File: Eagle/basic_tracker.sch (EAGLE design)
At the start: 21 parts, among them CN1 BATTERY, IC1 MCP1700 3.3v, X1 SMA

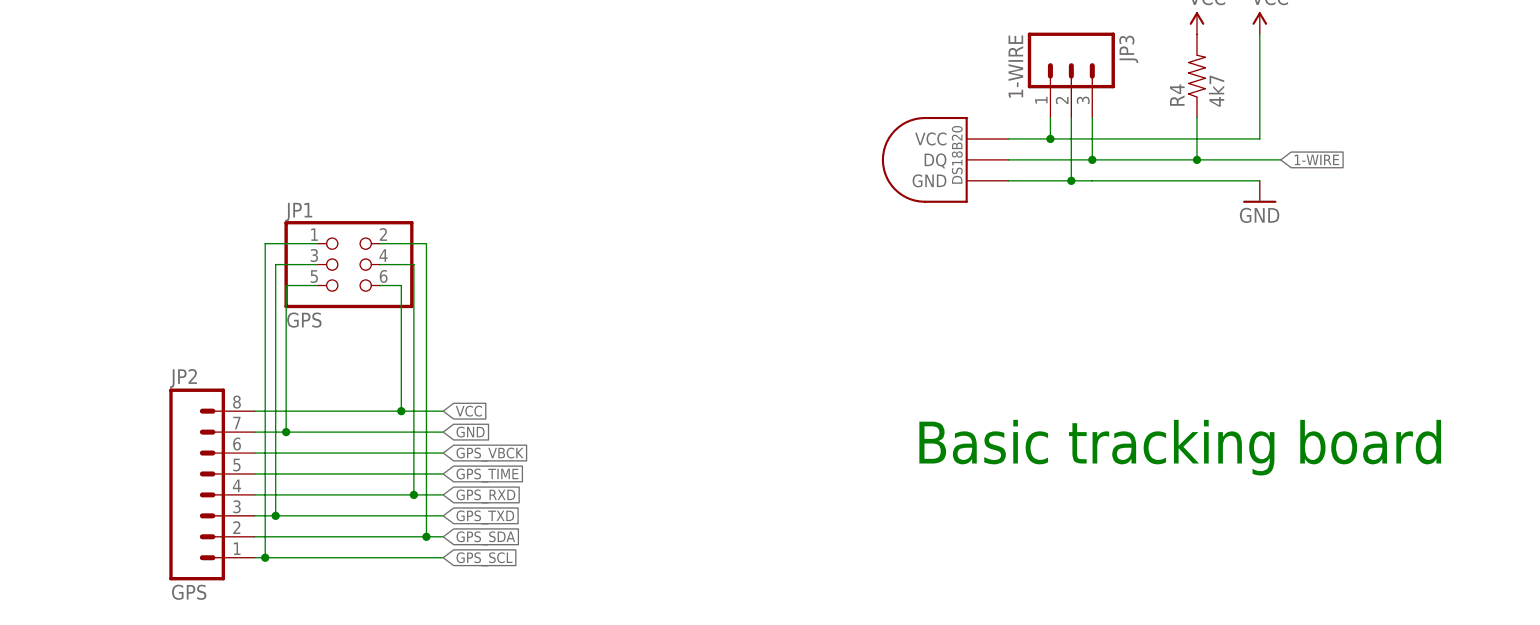
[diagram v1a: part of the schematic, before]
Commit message: Added a slightly modified version of the CAM file, tweaked the board and rerouted a few traces by hand
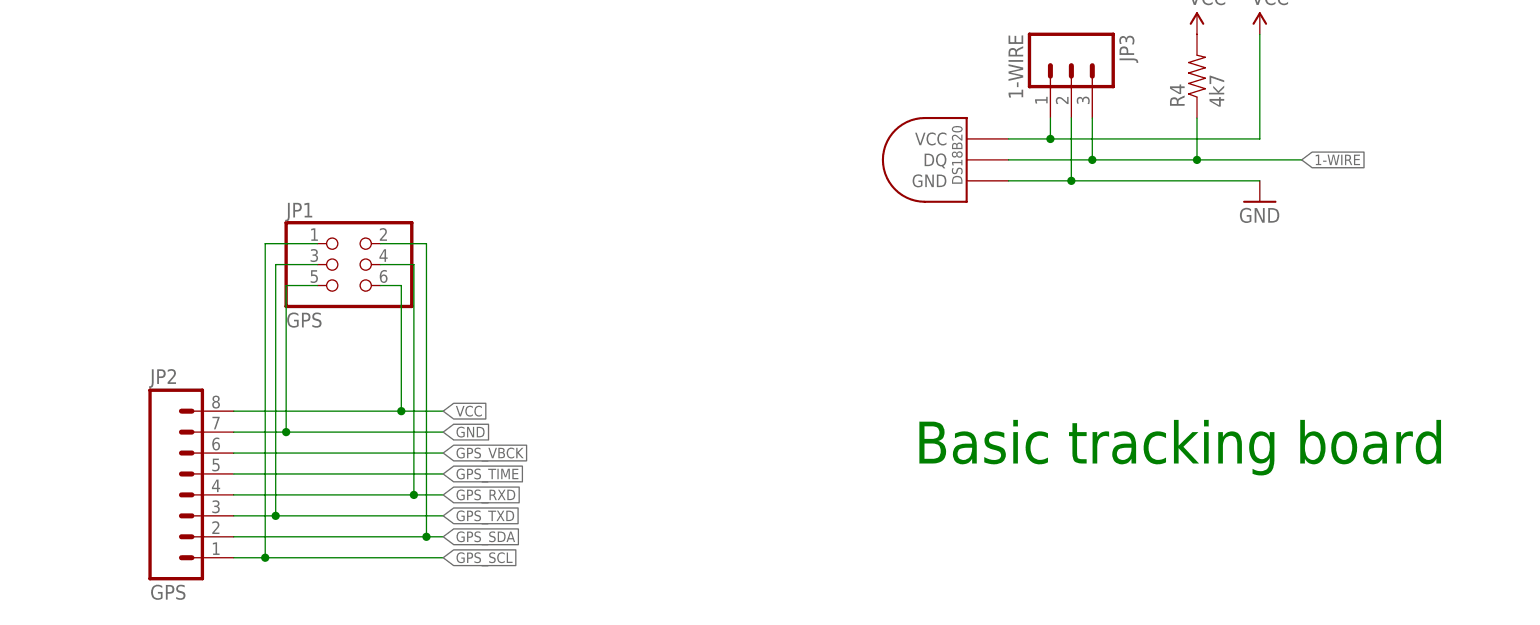
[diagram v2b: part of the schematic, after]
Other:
- moved on the sheet: JP2
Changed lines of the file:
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@@
 <grid distance="0.1" unitdist="inch" unit="inch" style="lines" multiple="1" display="no" altdistance="0.01" altunitdist="inch" altunit="inch"/>
 <layers>
-<layer number="1" name="Top" color="4" fill="1" visible="no" active="no"/>
-<layer number="16" name="Bottom" color="1" fill="1" visible="no" active="no"/>
-<layer number="17" name="Pads" color="2" fill="1" visible="no" active="no"/>
-<layer number="18" name="Vias" color="2" fill="1" visible="no" active="no"/>
-<layer number="19" name="Unrouted" color="6" fill="1" visible="no" active="no"/>
-<layer number="20" name="Dimension" color="7" fill="1" visible="no" active="no"/>
-<layer number="21" name="tPlace" color="16" fill="1" visible="no" active="no"/>
-<layer number="22" name="bPlace" color="14" fill="1" visible="no" active="no"/>
-<layer number="23" name="tOrigins" color="15" fill="1" visible="no" active="no"/>
-<layer number="24" name="bOrigins" color="15" fill="1" visible="no" active="no"/>
-<layer number="25" name="tNames" color="7" fill="1" visible="no" active="no"/>
-<layer number="26" name="bNames" color="7" fill="1" visible="no" active="no"/>
-<layer number="27" name="tValues" color="7" fill="1" visible="no" active="no"/>
-<layer number="28" name="bValues" color="7" fill="1" visible="no" active="no"/>
+<layer number="1" name="Top" color="4" fill="1" visible="yes" active="no"/>
+<layer number="16" name="Bottom" color="1" fill="1" visible="yes" active="no"/>
+<layer number="17" name="Pads" color="2" fill="1" visible="yes" active="no"/>
+<layer number="18" name="Vias" color="2" fill="1" visible="yes" active="no"/>
+<layer number="19" name="Unrouted" color="6" fill="1" visible="yes" active="no"/>
+<layer number="20" name="Dimension" color="15" fill="1" visible="yes" active="no"/>
+<layer number="21" name="tPlace" color="14" fill="1" visible="yes" active="no"/>
+<layer number="22" name="bPlace" color="7" fill="1" visible="yes" active="no"/>
+<layer number="23" name="tOrigins" color="15" fill="1" visible="yes" active="no"/>
+<layer number="24" name="bOrigins" color="15" fill="1" visible="yes" active="no"/>
+<layer number="25" name="tNames" color="7" fill="1" visible="yes" active="no"/>
+<layer number="26" name="bNames" color="7" fill="1" visible="yes" active="no"/>
+<layer number="27" name="tValues" color="7" fill="1" visible="yes" active="no"/>
+<layer number="28" name="bValues" color="7" fill="1" visible="yes" active="no"/>
 <layer number="29" name="tStop" color="7" fill="3" visible="no" active="no"/>
 <layer number="30" name="bStop" color="7" fill="6" visible="no" active="no"/>
-<layer number="31" name="tCream" color="11" fill="4" visible="no" active="no"/>
+<layer number="31" name="tCream" color="7" fill="4" visible="no" active="no"/>
 <layer number="32" name="bCream" color="7" fill="5" visible="no" active="no"/>
 <layer number="33" name="tFinish" color="6" fill="3" visible="no" active="no"/>
@@
 <layer number="35" name="tGlue" color="7" fill="4" visible="no" active="no"/>
 <layer number="36" name="bGlue" color="7" fill="5" visible="no" active="no"/>
-<layer number="37" name="tTest" color="7" fill="1" visible="no" active="no"/>
-<layer number="38" name="bTest" color="7" fill="1" visible="no" active="no"/>
+<layer number="37" name="tTest" color="7" fill="1" visible="yes" active="no"/>
+<layer number="38" name="bTest" color="7" fill="1" visible="yes" active="no"/>
 <layer number="39" name="tKeepout" color="4" fill="11" visible="no" active="no"/>
 <layer number="40" name="bKeepout" color="1" fill="11" visible="no" active="no"/>
@@
 <layer number="44" name="Drills" color="7" fill="1" visible="no" active="no"/>
 <layer number="45" name="Holes" color="7" fill="1" visible="no" active="no"/>
-<layer number="46" name="Milling" color="3" fill="1" visible="no" active="no"/>
-<layer number="47" name="Measures" color="7" fill="1" visible="no" active="no"/>
-<layer number="48" name="Document" color="7" fill="1" visible="no" active="no"/>
-<layer number="49" name="Reference" color="13" fill="1" visible="no" active="no"/>
-<layer number="50" name="dxf" color="7" fill="1" visible="no" active="no"/>
-<layer number="51" name="tDocu" color="14" fill="1" visible="no" active="no"/>
-<layer number="52" name="bDocu" color="7" fill="1" visible="no" active="no"/>
-<layer number="53" name="tGND_GNDA" color="7" fill="9" visible="no" active="no"/>
-<layer number="54" name="bGND_GNDA" color="1" fill="9" visible="no" active="no"/>
-<layer number="56" name="wert" color="7" fill="1" visible="no" active="no"/>
+<layer number="46" name="Milling" color="3" fill="1" visible="yes" active="no"/>
+<layer number="47" name="Measures" color="7" fill="1" visible="yes" active="no"/>
+<layer number="48" name="Document" color="7" fill="1" visible="yes" active="no"/>
+<layer number="49" name="Reference" color="7" fill="1" visible="yes" active="no"/>
+<layer number="50" name="dxf" color="7" fill="1" visible="yes" active="no"/>
+<layer number="51" name="tDocu" color="14" fill="1" visible="yes" active="no"/>
+<layer number="52" name="bDocu" color="7" fill="1" visible="yes" active="no"/>
+<layer number="53" name="tGND_GNDA" color="7" fill="9" visible="yes" active="no"/>
+<layer number="54" name="bGND_GNDA" color="1" fill="9" visible="yes" active="no"/>
+<layer number="56" name="wert" color="7" fill="1" visible="yes" active="no"/>
 <layer number="91" name="Nets" color="2" fill="1" visible="yes" active="yes"/>
 <layer number="92" name="Busses" color="1" fill="1" visible="yes" active="yes"/>
@@
 <instance part="GND10" gate="1" x="147.32" y="86.36"/>
 <instance part="LED1" gate="G$1" x="147.32" y="96.52"/>
-<instance part="JP2" gate="G$1" x="96.52" y="22.86"/>
+<instance part="JP2" gate="G$1" x="93.98" y="22.86"/>
 <instance part="C1" gate="G$1" x="81.28" y="152.4"/>
 <instance part="C2" gate="G$1" x="106.68" y="152.4"/>
@@
 <segment>
 <pinref part="JP2" gate="G$1" pin="8"/>
-<wire x1="101.6" y1="33.02" x2="119.38" y2="33.02" width="0.1524" layer="91"/>
+<wire x1="99.06" y1="33.02" x2="119.38" y2="33.02" width="0.1524" layer="91"/>
 <label x="124.46" y="33.02" size="1.27" layer="95" xref="yes"/>
 <pinref part="JP1" gate="A" pin="6"/>
@@
 <pinref part="GND6" gate="1" pin="GND"/>
 <wire x1="193.04" y1="60.96" x2="200.66" y2="60.96" width="0.1524" layer="91"/>
-<wire x1="200.66" y1="60.96" x2="203.2" y2="60.96" width="0.1524" layer="91"/>
-<wire x1="203.2" y1="60.96" x2="223.52" y2="60.96" width="0.1524" layer="91"/>
+<wire x1="200.66" y1="60.96" x2="223.52" y2="60.96" width="0.1524" layer="91"/>
 <pinref part="JP3" gate="G$1" pin="2"/>
 <wire x1="200.66" y1="68.58" x2="200.66" y2="60.96" width="0.1524" layer="91"/>
@@
 <segment>
 <pinref part="JP2" gate="G$1" pin="7"/>
-<wire x1="101.6" y1="30.48" x2="105.41" y2="30.48" width="0.1524" layer="91"/>
+<wire x1="99.06" y1="30.48" x2="105.41" y2="30.48" width="0.1524" layer="91"/>
 <label x="124.46" y="30.48" size="1.27" layer="95" xref="yes"/>
 <pinref part="JP1" gate="A" pin="5"/>
@@
 <segment>
 <pinref part="U$2" gate="G$1" pin="DQ"/>
-<wire x1="193.04" y1="63.5" x2="200.66" y2="63.5" width="0.1524" layer="91"/>
+<wire x1="193.04" y1="63.5" x2="203.2" y2="63.5" width="0.1524" layer="91"/>
 <pinref part="R4" gate="G$1" pin="1"/>
-<wire x1="200.66" y1="63.5" x2="203.2" y2="63.5" width="0.1524" layer="91"/>
 <wire x1="203.2" y1="63.5" x2="215.9" y2="63.5" width="0.1524" layer="91"/>
-<wire x1="215.9" y1="63.5" x2="226.06" y2="63.5" width="0.1524" layer="91"/>
+<wire x1="215.9" y1="63.5" x2="228.6" y2="63.5" width="0.1524" layer="91"/>
 <wire x1="215.9" y1="68.58" x2="215.9" y2="63.5" width="0.1524" layer="91"/>
 <junction x="215.9" y="63.5"/>
-<label x="226.06" y="63.5" size="1.27" layer="95" xref="yes"/>
+<label x="228.6" y="63.5" size="1.27" layer="95" xref="yes"/>
 <pinref part="JP3" gate="G$1" pin="3"/>
 <wire x1="203.2" y1="68.58" x2="203.2" y2="63.5" width="0.1524" layer="91"/>
@@
 <segment>
 <pinref part="JP2" gate="G$1" pin="6"/>
-<wire x1="101.6" y1="27.94" x2="124.46" y2="27.94" width="0.1524" layer="91"/>
+<wire x1="99.06" y1="27.94" x2="124.46" y2="27.94" width="0.1524" layer="91"/>
 <label x="124.46" y="27.94" size="1.27" layer="95" xref="yes"/>
 </segment>
@@
 <segment>
 <pinref part="JP2" gate="G$1" pin="5"/>
-<wire x1="101.6" y1="25.4" x2="124.46" y2="25.4" width="0.1524" layer="91"/>
+<wire x1="99.06" y1="25.4" x2="124.46" y2="25.4" width="0.1524" layer="91"/>
 <label x="124.46" y="25.4" size="1.27" layer="95" xref="yes"/>
 </segment>
@@
 <segment>
 <pinref part="JP2" gate="G$1" pin="4"/>
-<wire x1="101.6" y1="22.86" x2="120.904" y2="22.86" width="0.1524" layer="91"/>
+<wire x1="99.06" y1="22.86" x2="120.904" y2="22.86" width="0.1524" layer="91"/>
 <label x="124.46" y="22.86" size="1.27" layer="95" xref="yes"/>
 <pinref part="JP1" gate="A" pin="4"/>
@@
 <segment>
 <pinref part="JP2" gate="G$1" pin="3"/>
-<wire x1="101.6" y1="20.32" x2="104.14" y2="20.32" width="0.1524" layer="91"/>
+<wire x1="99.06" y1="20.32" x2="104.14" y2="20.32" width="0.1524" layer="91"/>
 <label x="124.46" y="20.32" size="1.27" layer="95" xref="yes"/>
 <pinref part="JP1" gate="A" pin="3"/>
@@
 <segment>
 <pinref part="JP2" gate="G$1" pin="2"/>
-<wire x1="101.6" y1="17.78" x2="122.428" y2="17.78" width="0.1524" layer="91"/>
+<wire x1="99.06" y1="17.78" x2="122.428" y2="17.78" width="0.1524" layer="91"/>
 <label x="124.46" y="17.78" size="1.27" layer="95" xref="yes"/>
 <pinref part="JP1" gate="A" pin="2"/>
@@
 <segment>
 <pinref part="JP2" gate="G$1" pin="1"/>
-<wire x1="101.6" y1="15.24" x2="102.87" y2="15.24" width="0.1524" layer="91"/>
+<wire x1="99.06" y1="15.24" x2="102.87" y2="15.24" width="0.1524" layer="91"/>
 <label x="124.46" y="15.24" size="1.27" layer="95" xref="yes"/>
 <pinref part="JP1" gate="A" pin="1"/>
